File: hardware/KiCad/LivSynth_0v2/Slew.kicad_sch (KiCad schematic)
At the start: 8 parts, among them J17 Jumper, U8 TL074

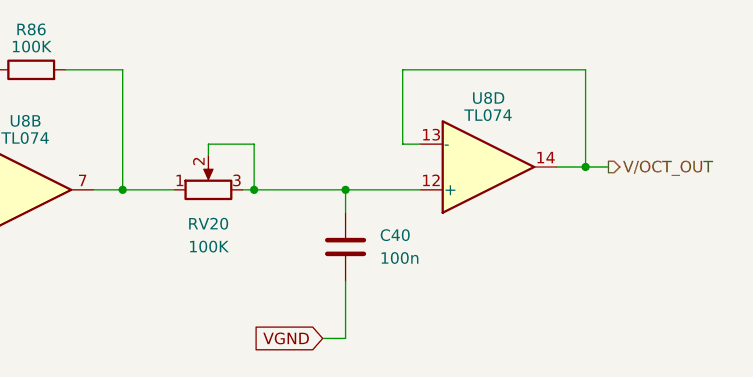
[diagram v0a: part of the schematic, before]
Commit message: Analog redesign:  - Power: Add voltage and current test points  - MCU: use PA11/PA12 for USB DFU interface  - MCU: add NRST reset switch  - Slew: increase portamento cap  - VCO: invert trim pots  - VCF: let resonance kick in earlier  - VCF: invert pots  - VCA: invert trim pot  - EG: full redesign, properly referencing VGND now  - LFO: R61 = 51K  - ModMatrix: add EG attenuverters  - IO: invert pots  - IO: limit output gain for 1W speaker  - IO: connect BTN_SHIFT in gap free order to SR
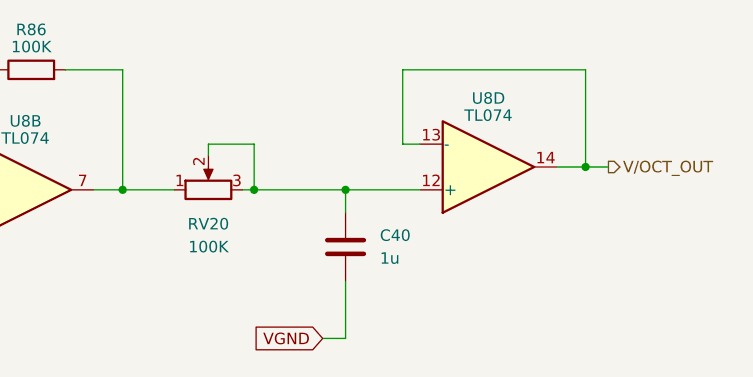
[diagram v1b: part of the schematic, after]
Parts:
- C40: value 100n -> 1u
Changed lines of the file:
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@@
       (effects (font (size 1.27 1.27)) (justify left))
     )
-    (property "Value" "100n" (id 1) (at 200.66 103.5049 0)
+    (property "Value" "1u" (id 1) (at 200.66 103.5049 0)
       (effects (font (size 1.27 1.27)) (justify left))
     )

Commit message: Analog Redesign:  - Power: Build ververse polarity protection using P-Mosfet and Zener Diode      - (https://www.youtube.com/watch?v=Ltx4vovY5Z4 - 1:28)  - Power: Build adjustable buck regulator for 8-9V stable voltage source  - PCB: Add location for order number ("JLCJLCJLCJLC")  - General: Add Tooling Holes for PCB assembly  - PCB: check frontend component layout for symmetry  - VCF: fix sound issues  - PCB: Add SloBlo icon  - PCB: Add switch labels to front side  - EG: test new design  - MCU: Add some debug pins
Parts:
- U8: LCSC (none) -> C2057504
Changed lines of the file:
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@@
+      (effects (font (size 1.27 1.27)) hide)
+    )
+    (property "LCSC" "C2057504" (id 4) (at 161.29 95.885 0)
       (effects (font (size 1.27 1.27)) hide)
     )
@@
       (effects (font (size 1.27 1.27)) hide)
     )
+    (property "LCSC" "C2057504" (id 4) (at 212.725 93.345 0)
+      (effects (font (size 1.27 1.27)) hide)
+    )

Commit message: progress 2023-01-21
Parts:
- renumbered U8 to U3
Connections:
- net V/OCT_OUT: now also U3.8, U3.9 (-); no longer U3.13 (-), U3.14
- net at C40.1, RV20.2, RV20.3: now also U3.10 (+); no longer U3.12 (+)
- net at R83.2, R85.2: now also U8.10 (+); no longer U8.5 (+)
- net at R84.2, R86.1: now also U8.9 (-); no longer U8.6 (-)
- net at R86.2, RV20.1: now also U8.8; no longer U8.7
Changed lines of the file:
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@@
     (pin "2")
   )
-  (symbol (lib_id "Amplifier_Operational:TL074") (at 161.29 95.885 0) (mirror x) (unit 2)
+  (symbol (lib_id "Amplifier_Operational:TL074") (at 161.29 95.885 0) (mirror x) (unit 3)
     (in_bom yes) (on_board yes)
     (property "Reference" "U8" (id 0) (at 161.29 88.265 0))
@@
     (pin "2")
   )
-  (symbol (lib_id "Amplifier_Operational:TL074") (at 212.725 93.345 0) (mirror x) (unit 4)
+  (symbol (lib_id "Amplifier_Operational:TL074") (at 212.725 93.345 0) (mirror x) (unit 3)
     (in_bom yes) (on_board yes)
-    (property "Reference" "U8" (id 0) (at 212.725 85.725 0))
+    (property "Reference" "U3" (id 0) (at 212.725 85.725 0))
     (property "Value" "TL074" (id 1) (at 212.725 87.63 0))
     (property "Footprint" "Package_SO:SOIC-14_3.9x8.7mm_P1.27mm" (id 2) (at 211.455 95.885 0)

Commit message: LCSC component looked up
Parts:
- C40: footprint Capacitor_THT:C_Rect_L7.2mm_W2.5mm_P5.00mm_FKS2_FKP2_MKS2_MKP2 -> Capacitor_THT:C_Rect_L7.2mm_W5.5mm_P5.00mm_FKS2_FKP2_MKS2_MKP2
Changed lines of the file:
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@@
       (effects (font (size 1.27 1.27)) (justify left))
     )
-    (property "Footprint" "Capacitor_THT:C_Rect_L7.2mm_W2.5mm_P5.00mm_FKS2_FKP2_MKS2_MKP2" (id 2) (at 197.8152 106.045 0)
+    (property "Footprint" "Capacitor_THT:C_Rect_L7.2mm_W5.5mm_P5.00mm_FKS2_FKP2_MKS2_MKP2" (id 2) (at 197.8152 106.045 0)
       (effects (font (size 1.27 1.27)) hide)
     )

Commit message: Geographical reannotate
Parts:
- renumbered C40 to C19, J17 to J22, R84 to R82, R86 to R83, R85 to R84, R83 to R87, U3 to U4, U8 to U6
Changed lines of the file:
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@@
   (symbol (lib_id "Device:C") (at 196.85 102.235 0) (unit 1)
     (in_bom yes) (on_board yes) (fields_autoplaced)
-    (property "Reference" "C40" (id 0) (at 200.66 100.9649 0)
+    (property "Reference" "C19" (id 0) (at 200.66 100.9649 0)
       (effects (font (size 1.27 1.27)) (justify left))
     )
@@
   (symbol (lib_id "Device:R") (at 144.78 98.425 90) (unit 1)
     (in_bom yes) (on_board yes)
-    (property "Reference" "R83" (id 0) (at 144.78 102.87 90))
+    (property "Reference" "R87" (id 0) (at 144.78 102.87 90))
     (property "Value" "100K" (id 1) (at 144.78 100.965 90))
     (property "Footprint" "Resistor_THT:R_Axial_DIN0207_L6.3mm_D2.5mm_P7.62mm_Horizontal" (id 2) (at 144.78 100.203 90)
@@
   (symbol (lib_id "Amplifier_Operational:TL074") (at 161.29 95.885 0) (mirror x) (unit 3)
     (in_bom yes) (on_board yes)
-    (property "Reference" "U8" (id 0) (at 161.29 88.265 0))
+    (property "Reference" "U6" (id 0) (at 161.29 88.265 0))
     (property "Value" "TL074" (id 1) (at 161.29 90.17 0))
     (property "Footprint" "Package_SO:SOIC-14_3.9x8.7mm_P1.27mm" (id 2) (at 160.02 98.425 0)
@@
   (symbol (lib_id "Device:R") (at 161.925 82.55 90) (unit 1)
     (in_bom yes) (on_board yes)
-    (property "Reference" "R86" (id 0) (at 161.925 78.105 90))
+    (property "Reference" "R83" (id 0) (at 161.925 78.105 90))
     (property "Value" "100K" (id 1) (at 161.925 80.01 90))
     (property "Footprint" "Resistor_THT:R_Axial_DIN0207_L6.3mm_D2.5mm_P7.62mm_Horizontal" (id 2) (at 161.925 84.328 90)
@@
   (symbol (lib_id "Connector:Conn_01x02_Male") (at 121.285 93.345 90) (mirror x) (unit 1)
     (in_bom yes) (on_board yes) (fields_autoplaced)
-    (property "Reference" "J17" (id 0) (at 125.73 92.7099 90)
+    (property "Reference" "J22" (id 0) (at 125.73 92.7099 90)
       (effects (font (size 1.27 1.27)) (justify right))
     )
@@
   (symbol (lib_id "Amplifier_Operational:TL074") (at 212.725 93.345 0) (mirror x) (unit 3)
     (in_bom yes) (on_board yes)
-    (property "Reference" "U3" (id 0) (at 212.725 85.725 0))
+    (property "Reference" "U4" (id 0) (at 212.725 85.725 0))
     (property "Value" "TL074" (id 1) (at 212.725 87.63 0))
     (property "Footprint" "Package_SO:SOIC-14_3.9x8.7mm_P1.27mm" (id 2) (at 211.455 95.885 0)
@@
   (symbol (lib_id "Device:R") (at 144.78 93.345 90) (unit 1)
     (in_bom yes) (on_board yes)
-    (property "Reference" "R84" (id 0) (at 144.78 88.9 90))
+    (property "Reference" "R82" (id 0) (at 144.78 88.9 90))
     (property "Value" "100K" (id 1) (at 144.78 90.805 90))
     (property "Footprint" "Resistor_THT:R_Axial_DIN0207_L6.3mm_D2.5mm_P7.62mm_Horizontal" (id 2) (at 144.78 95.123 90)
@@
   (symbol (lib_id "Device:R") (at 151.765 106.045 180) (unit 1)
     (in_bom yes) (on_board yes)
-    (property "Reference" "R85" (id 0) (at 147.32 106.045 90))
+    (property "Reference" "R84" (id 0) (at 147.32 106.045 90))
     (property "Value" "330K" (id 1) (at 149.225 106.045 90))
     (property "Footprint" "Resistor_THT:R_Axial_DIN0207_L6.3mm_D2.5mm_P7.62mm_Horizontal" (id 2) (at 153.543 106.045 90)
